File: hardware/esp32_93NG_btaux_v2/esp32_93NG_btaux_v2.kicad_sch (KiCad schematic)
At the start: 4 parts

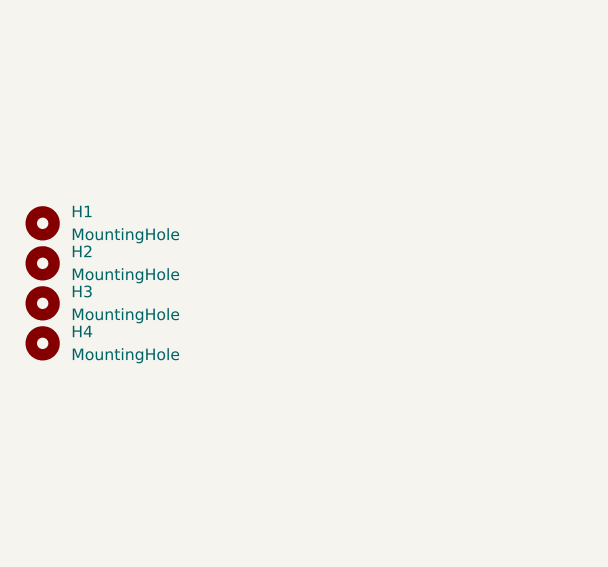
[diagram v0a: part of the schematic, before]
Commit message: Added top and bottom faceplates. Improved silkscreen labels for pinouts, buttons, connectors.
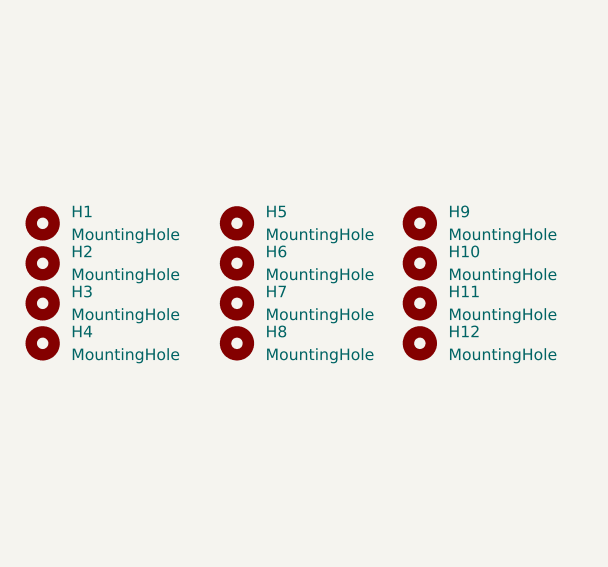
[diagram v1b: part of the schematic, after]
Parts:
- added H10, H11, H12, H5, H6, H7, H8, H9: MountingHole, kicadlibrary:MountingHole_3.2mm_M3_BARE, symbol Mechanical:MountingHole
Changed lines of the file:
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@@
 (kicad_sch (version 20211123) (generator eeschema)
   (paper "A4")
+  (symbol (lib_id "Mechanical:MountingHole") (at 236.22 78.74 0) (unit 1)
+    (in_bom yes) (on_board yes) (fields_autoplaced)
+    (property "Reference" "H12" (id 0) (at 239.395 77.4699 0)
+      (effects (font (size 1.27 1.27)) (justify left))
+    )
+    (property "Value" "MountingHole" (id 1) (at 239.395 80.0099 0)
+      (effects (font (size 1.27 1.27)) (justify left))
+    )
+    (property "Footprint" "kicadlibrary:MountingHole_3.2mm_M3_BARE" (id 2) (at 236.22 78.74 0)
+      (effects (font (size 1.27 1.27)) hide)
+    )
+    (property "Datasheet" "~" (id 3) (at 236.22 78.74 0)
+      (effects (font (size 1.27 1.27)) hide)
+    )
+  )
   (symbol (lib_id "Mechanical:MountingHole") (at 194.31 78.74 0) (unit 1)
     (in_bom yes) (on_board yes) (fields_autoplaced)
@@
     )
   )
+  (symbol (lib_id "Mechanical:MountingHole") (at 215.9 78.74 0) (unit 1)
+    (in_bom yes) (on_board yes) (fields_autoplaced)
+    (property "Reference" "H8" (id 0) (at 219.075 77.4699 0)
+      (effects (font (size 1.27 1.27)) (justify left))
+    )
+    (property "Value" "MountingHole" (id 1) (at 219.075 80.0099 0)
+      (effects (font (size 1.27 1.27)) (justify left))
+    )
+    (property "Footprint" "kicadlibrary:MountingHole_3.2mm_M3_BARE" (id 2) (at 215.9 78.74 0)
+      (effects (font (size 1.27 1.27)) hide)
+    )
+    (property "Datasheet" "~" (id 3) (at 215.9 78.74 0)
+      (effects (font (size 1.27 1.27)) hide)
+    )
+  )
+  (symbol (lib_id "Mechanical:MountingHole") (at 215.9 74.295 0) (unit 1)
+    (in_bom yes) (on_board yes) (fields_autoplaced)
+    (property "Reference" "H7" (id 0) (at 219.075 73.0249 0)
+      (effects (font (size 1.27 1.27)) (justify left))
+    )
+    (property "Value" "MountingHole" (id 1) (at 219.075 75.5649 0)
+      (effects (font (size 1.27 1.27)) (justify left))
+    )
+    (property "Footprint" "kicadlibrary:MountingHole_3.2mm_M3_BARE" (id 2) (at 215.9 74.295 0)
+      (effects (font (size 1.27 1.27)) hide)
+    )
+    (property "Datasheet" "~" (id 3) (at 215.9 74.295 0)
+      (effects (font (size 1.27 1.27)) hide)
+    )
+  )
   (symbol (lib_id "Mechanical:MountingHole") (at 194.31 69.85 0) (unit 1)
     (in_bom yes) (on_board yes) (fields_autoplaced)
@@
     )
   )
+  (symbol (lib_id "Mechanical:MountingHole") (at 215.9 69.85 0) (unit 1)
+    (in_bom yes) (on_board yes) (fields_autoplaced)
+    (property "Reference" "H6" (id 0) (at 219.075 68.5799 0)
+      (effects (font (size 1.27 1.27)) (justify left))
+    )
+    (property "Value" "MountingHole" (id 1) (at 219.075 71.1199 0)
+      (effects (font (size 1.27 1.27)) (justify left))
+    )
+    (property "Footprint" "kicadlibrary:MountingHole_3.2mm_M3_BARE" (id 2) (at 215.9 69.85 0)
+      (effects (font (size 1.27 1.27)) hide)
+    )
+    (property "Datasheet" "~" (id 3) (at 215.9 69.85 0)
+      (effects (font (size 1.27 1.27)) hide)
+    )
+  )
   (symbol (lib_id "Mechanical:MountingHole") (at 194.31 65.405 0) (unit 1)
     (in_bom yes) (on_board yes) (fields_autoplaced)
@@
     )
     (property "Datasheet" "~" (id 3) (at 194.31 65.405 0)
+      (effects (font (size 1.27 1.27)) hide)
+    )
+  )
+  (symbol (lib_id "Mechanical:MountingHole") (at 215.9 65.405 0) (unit 1)
+    (in_bom yes) (on_board yes) (fields_autoplaced)
+    (property "Reference" "H5" (id 0) (at 219.075 64.1349 0)
+      (effects (font (size 1.27 1.27)) (justify left))
+    )
+    (property "Value" "MountingHole" (id 1) (at 219.075 66.6749 0)
+      (effects (font (size 1.27 1.27)) (justify left))
+    )
+    (property "Footprint" "kicadlibrary:MountingHole_3.2mm_M3_BARE" (id 2) (at 215.9 65.405 0)
+      (effects (font (size 1.27 1.27)) hide)
+    )
+    (property "Datasheet" "~" (id 3) (at 215.9 65.405 0)
+      (effects (font (size 1.27 1.27)) hide)
+    )
+  )
+  (symbol (lib_id "Mechanical:MountingHole") (at 236.22 74.295 0) (unit 1)
+    (in_bom yes) (on_board yes) (fields_autoplaced)
+    (property "Reference" "H11" (id 0) (at 239.395 73.0249 0)
+      (effects (font (size 1.27 1.27)) (justify left))
+    )
+    (property "Value" "MountingHole" (id 1) (at 239.395 75.5649 0)
+      (effects (font (size 1.27 1.27)) (justify left))
+    )
+    (property "Footprint" "kicadlibrary:MountingHole_3.2mm_M3_BARE" (id 2) (at 236.22 74.295 0)
+      (effects (font (size 1.27 1.27)) hide)
+    )
+    (property "Datasheet" "~" (id 3) (at 236.22 74.295 0)
+      (effects (font (size 1.27 1.27)) hide)
+    )
+  )
+  (symbol (lib_id "Mechanical:MountingHole") (at 236.22 65.405 0) (unit 1)
+    (in_bom yes) (on_board yes) (fields_autoplaced)
+    (property "Reference" "H9" (id 0) (at 239.395 64.1349 0)
+      (effects (font (size 1.27 1.27)) (justify left))
+    )
+    (property "Value" "MountingHole" (id 1) (at 239.395 66.6749 0)
+      (effects (font (size 1.27 1.27)) (justify left))
+    )
+    (property "Footprint" "kicadlibrary:MountingHole_3.2mm_M3_BARE" (id 2) (at 236.22 65.405 0)
+      (effects (font (size 1.27 1.27)) hide)
+    )
+    (property "Datasheet" "~" (id 3) (at 236.22 65.405 0)
+      (effects (font (size 1.27 1.27)) hide)
+    )
+  )
+  (symbol (lib_id "Mechanical:MountingHole") (at 236.22 69.85 0) (unit 1)
+    (in_bom yes) (on_board yes) (fields_autoplaced)
+    (property "Reference" "H10" (id 0) (at 239.395 68.5799 0)
+      (effects (font (size 1.27 1.27)) (justify left))
+    )
+    (property "Value" "MountingHole" (id 1) (at 239.395 71.1199 0)
+      (effects (font (size 1.27 1.27)) (justify left))
+    )
+    (property "Footprint" "kicadlibrary:MountingHole_3.2mm_M3_BARE" (id 2) (at 236.22 69.85 0)
+      (effects (font (size 1.27 1.27)) hide)
+    )
+    (property "Datasheet" "~" (id 3) (at 236.22 69.85 0)
       (effects (font (size 1.27 1.27)) hide)
     )
@@
       (reference "H4") (unit 1) (value "MountingHole") (footprint "kicadlibrary:MountingHole_3.2mm_M3_BARE")
     )
+    (path "/d4d4fa68-34f2-4653-bbf0-2d24f29cf971"
+      (reference "H5") (unit 1) (value "MountingHole") (footprint "kicadlibrary:MountingHole_3.2mm_M3_BARE")
+    )
+    (path "/b93d027f-21f6-4fc9-ad3f-317eded6973b"
+      (reference "H6") (unit 1) (value "MountingHole") (footprint "kicadlibrary:MountingHole_3.2mm_M3_BARE")
+    )
+    (path "/675b2a1e-1d1e-4f5b-91f1-23d348015a92"
+      (reference "H7") (unit 1) (value "MountingHole") (footprint "kicadlibrary:MountingHole_3.2mm_M3_BARE")
+    )
+    (path "/4a06368c-ac2a-4bd5-acce-393b80f8a278"
+      (reference "H8") (unit 1) (value "MountingHole") (footprint "kicadlibrary:MountingHole_3.2mm_M3_BARE")
+    )
+    (path "/d830daa2-a9b8-41c7-bef6-ed9486bc304b"
+      (reference "H9") (unit 1) (value "MountingHole") (footprint "kicadlibrary:MountingHole_3.2mm_M3_BARE")
+    )
+    (path "/fc01945a-0f3e-4ccb-869e-e232ff747d9c"
+      (reference "H10") (unit 1) (value "MountingHole") (footprint "kicadlibrary:MountingHole_3.2mm_M3_BARE")
+    )
+    (path "/d6a628a3-74f3-4e24-acf3-9de677b2a9a4"
+      (reference "H11") (unit 1) (value "MountingHole") (footprint "kicadlibrary:MountingHole_3.2mm_M3_BARE")
+    )
+    (path "/0e676034-93d3-40ce-ad67-094e6cf2ff98"
+      (reference "H12") (unit 1) (value "MountingHole") (footprint "kicadlibrary:MountingHole_3.2mm_M3_BARE")
+    )
     (path "/886f198d-d54b-48bc-876a-d12e0fc086d6/6ba6f66f-2911-4473-9f15-6c86b7f11d4c"

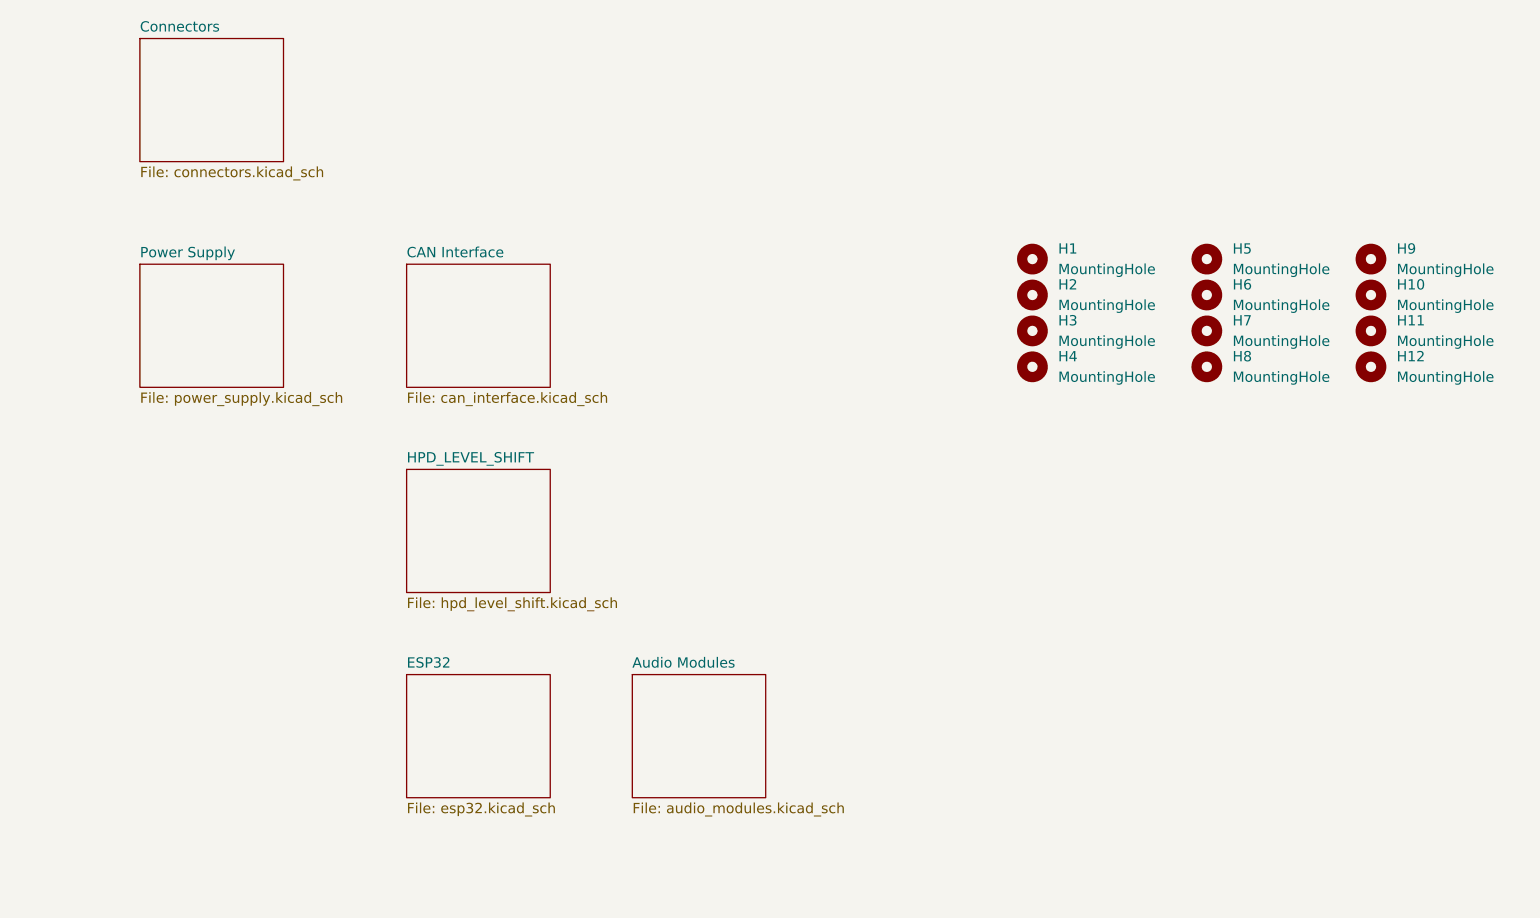
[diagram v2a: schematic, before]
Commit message: Updated silkscreen
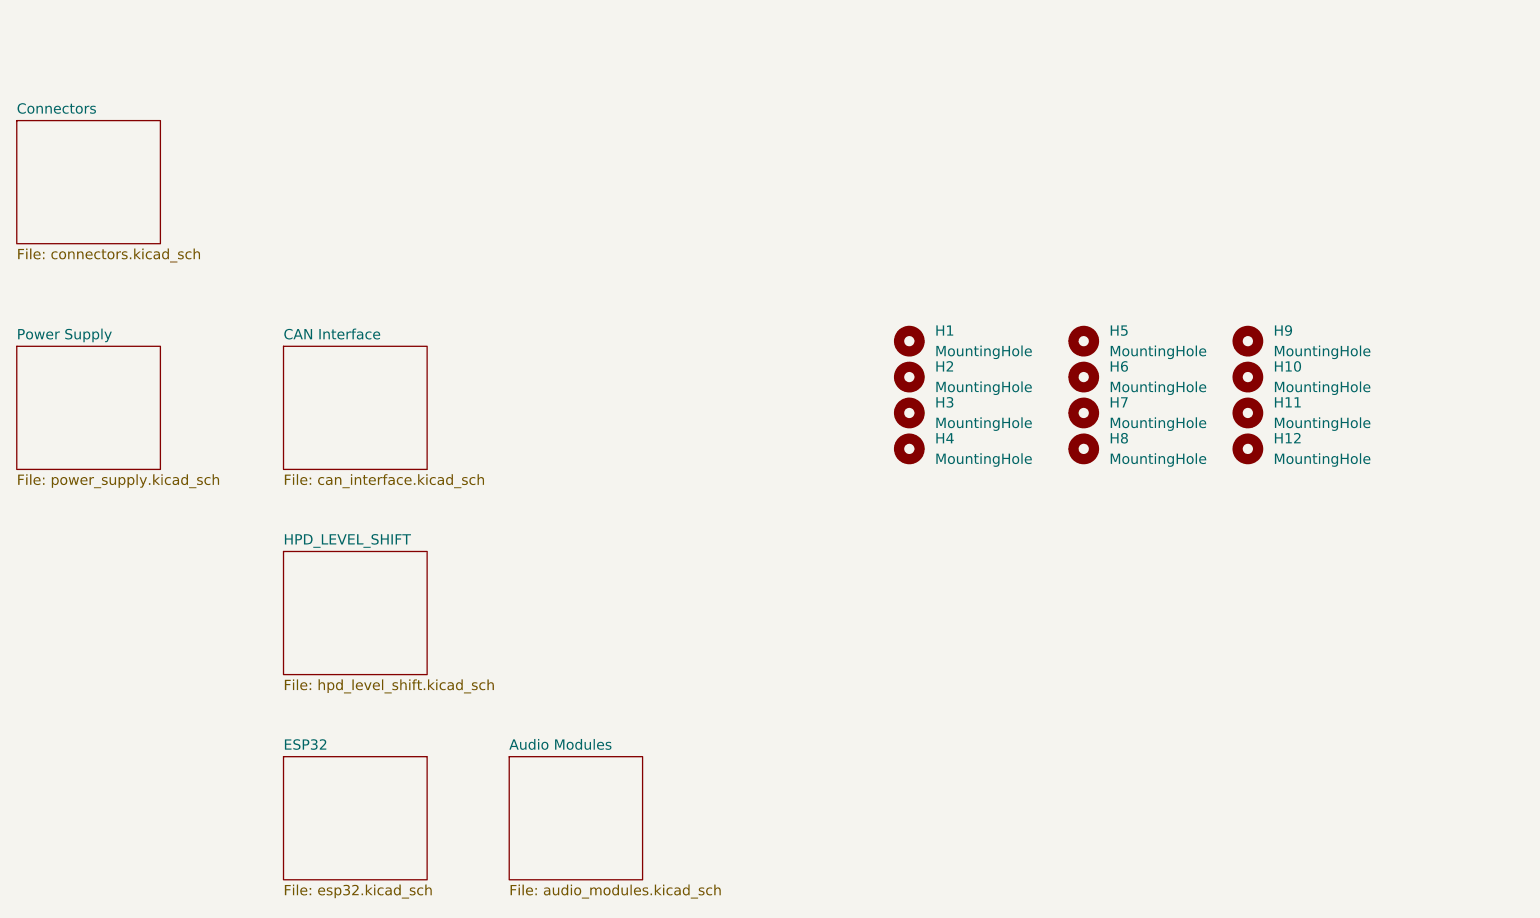
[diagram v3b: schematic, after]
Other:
- moved on the sheet: H1, H10, H11, H12, H2, H3, H4, H5, H6, H7, H8, H9
